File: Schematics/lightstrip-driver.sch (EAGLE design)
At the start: 11 parts, among them IC1 MCP2300X/P, Q1 FQP30N06L, Q2 FQP30N06L, Q3 FQP30N06L

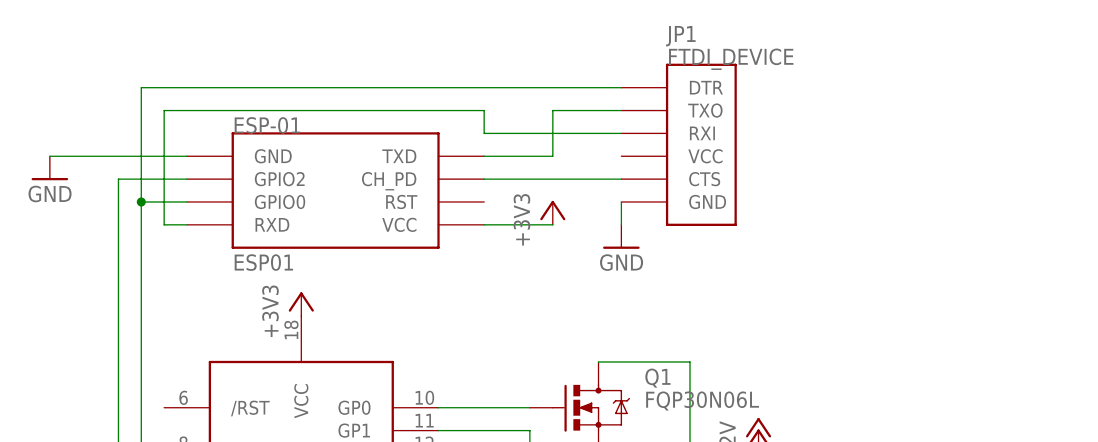
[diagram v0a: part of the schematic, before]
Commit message: Update board with correct ESP8266 autoreset connections
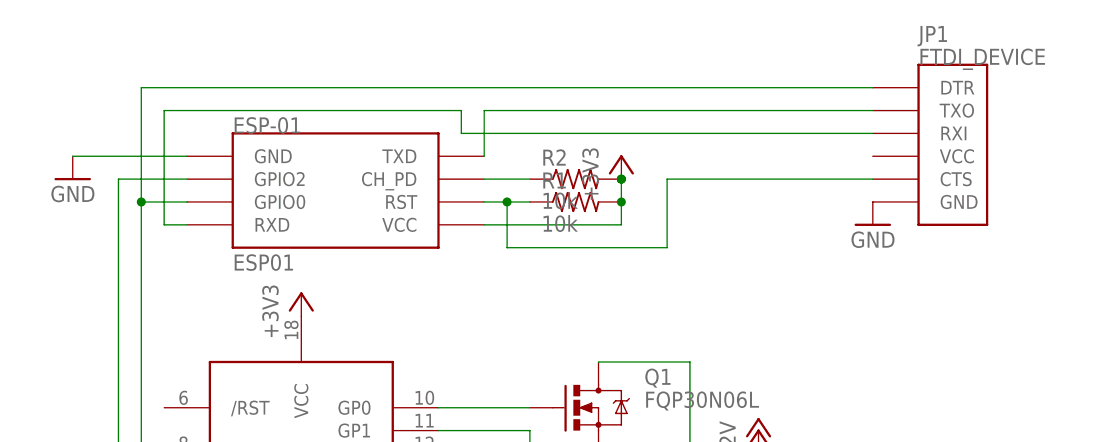
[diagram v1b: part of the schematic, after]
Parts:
- added R1, R2: 10k, resistor:R-US_0207/7
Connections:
- removed net N$10: ESP-01.CH_PD, JP1.CTS
- new net N$15: ESP-01.RST, JP1.CTS, R1.1
- new net N$3: ESP-01.CH_PD, R2.1
- net +3V3: now also R1.2, R2.2
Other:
- moved on the sheet: JP1
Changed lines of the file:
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@@
 <part name="GND9" library="supply1" deviceset="GND" device=""/>
 <part name="DC-IN" library="SparkFun-Connectors" deviceset="POWER_JACK" device="PTH"/>
+<part name="R1" library="resistor" deviceset="R-US_" device="0207/7" value="10k"/>
+<part name="R2" library="resistor" deviceset="R-US_" device="0207/7" value="10k"/>
 </parts>
 <sheets>
@@
 <instance part="+3V1" gate="G$1" x="-15.24" y="30.48"/>
 <instance part="GND2" gate="1" x="-25.4" y="15.24"/>
-<instance part="+3V2" gate="G$1" x="-55.88" y="104.14"/>
-<instance part="JP1" gate="G$1" x="-43.18" y="111.76"/>
-<instance part="GND3" gate="1" x="-48.26" y="99.06" rot="MR0"/>
+<instance part="+3V2" gate="G$1" x="-48.26" y="109.22"/>
+<instance part="JP1" gate="G$1" x="-15.24" y="111.76"/>
+<instance part="GND3" gate="1" x="-20.32" y="101.6" rot="MR0"/>
 <instance part="RGB" gate="G$1" x="-27.94" y="71.12" rot="R180"/>
 <instance part="P+2" gate="1" x="-33.02" y="78.74"/>
@@
 <instance part="P+4" gate="1" x="-76.2" y="22.86"/>
 <instance part="GND8" gate="1" x="-76.2" y="12.7"/>
-<instance part="GND9" gate="1" x="-111.76" y="106.68" rot="MR0"/>
+<instance part="GND9" gate="1" x="-109.22" y="106.68" rot="MR0"/>
 <instance part="DC-IN" gate="G$1" x="-45.72" y="15.24"/>
+<instance part="R1" gate="G$1" x="-53.34" y="104.14"/>
+<instance part="R2" gate="G$1" x="-53.34" y="106.68"/>
 </instances>
 <busses>
@@
 <pinref part="JP1" gate="G$1" pin="GND"/>
 <pinref part="GND3" gate="1" pin="GND"/>
-<wire x1="-48.26" y1="104.14" x2="-48.26" y2="101.6" width="0.1524" layer="91"/>
 </segment>
 <segment>
@@
 <pinref part="GND9" gate="1" pin="GND"/>
 <pinref part="ESP-01" gate="G$1" pin="GND"/>
-<wire x1="-111.76" y1="109.22" x2="-96.52" y2="109.22" width="0.1524" layer="91"/>
+<wire x1="-109.22" y1="109.22" x2="-96.52" y2="109.22" width="0.1524" layer="91"/>
 </segment>
 </net>
@@
 </segment>
 <segment>
-<pinref part="ESP-01" gate="G$1" pin="VCC"/>
-<pinref part="+3V2" gate="G$1" pin="+3V3"/>
-<wire x1="-63.5" y1="101.6" x2="-55.88" y2="101.6" width="0.1524" layer="91"/>
-</segment>
-<segment>
 <pinref part="IC1" gate="G$1" pin="VCC"/>
 <pinref part="+3V3" gate="G$1" pin="+3V3"/>
+</segment>
+<segment>
+<pinref part="+3V2" gate="G$1" pin="+3V3"/>
+<junction x="-48.26" y="106.68"/>
+<pinref part="R2" gate="G$1" pin="2"/>
+<wire x1="-48.26" y1="106.68" x2="-48.26" y2="104.14" width="0.1524" layer="91"/>
+<junction x="-48.26" y="106.68"/>
+<pinref part="R1" gate="G$1" pin="2"/>
+<pinref part="ESP-01" gate="G$1" pin="VCC"/>
+<wire x1="-63.5" y1="101.6" x2="-48.26" y2="101.6" width="0.1524" layer="91"/>
+<wire x1="-48.26" y1="101.6" x2="-48.26" y2="104.14" width="0.1524" layer="91"/>
+<junction x="-48.26" y="104.14"/>
 </segment>
 </net>
@@
 <wire x1="-96.52" y1="101.6" x2="-99.06" y2="101.6" width="0.1524" layer="91"/>
 <wire x1="-99.06" y1="101.6" x2="-99.06" y2="114.3" width="0.1524" layer="91"/>
-<wire x1="-99.06" y1="114.3" x2="-63.5" y2="114.3" width="0.1524" layer="91"/>
-<wire x1="-63.5" y1="114.3" x2="-63.5" y2="111.76" width="0.1524" layer="91"/>
-<wire x1="-63.5" y1="111.76" x2="-48.26" y2="111.76" width="0.1524" layer="91"/>
+<wire x1="-99.06" y1="114.3" x2="-66.04" y2="114.3" width="0.1524" layer="91"/>
+<wire x1="-66.04" y1="114.3" x2="-66.04" y2="111.76" width="0.1524" layer="91"/>
+<wire x1="-66.04" y1="111.76" x2="-20.32" y2="111.76" width="0.1524" layer="91"/>
 </segment>
 </net>
@@
 <segment>
 <pinref part="ESP-01" gate="G$1" pin="TXD"/>
-<wire x1="-63.5" y1="109.22" x2="-55.88" y2="109.22" width="0.1524" layer="91"/>
-<wire x1="-55.88" y1="109.22" x2="-55.88" y2="114.3" width="0.1524" layer="91"/>
-<wire x1="-55.88" y1="114.3" x2="-48.26" y2="114.3" width="0.1524" layer="91"/>
+<wire x1="-63.5" y1="109.22" x2="-63.5" y2="114.3" width="0.1524" layer="91"/>
+<wire x1="-63.5" y1="114.3" x2="-20.32" y2="114.3" width="0.1524" layer="91"/>
 <pinref part="JP1" gate="G$1" pin="TXO"/>
-</segment>
-</net>
-<net name="N$10" class="0">
-<segment>
-<pinref part="JP1" gate="G$1" pin="CTS"/>
-<pinref part="ESP-01" gate="G$1" pin="CH_PD"/>
-<wire x1="-48.26" y1="106.68" x2="-63.5" y2="106.68" width="0.1524" layer="91"/>
 </segment>
 </net>
@@
 <wire x1="-101.6" y1="116.84" x2="-101.6" y2="104.14" width="0.1524" layer="91"/>
 <junction x="-101.6" y="104.14"/>
-<wire x1="-101.6" y1="116.84" x2="-48.26" y2="116.84" width="0.1524" layer="91"/>
+<wire x1="-101.6" y1="116.84" x2="-20.32" y2="116.84" width="0.1524" layer="91"/>
 <pinref part="JP1" gate="G$1" pin="DTR"/>
 </segment>
@@
 </segment>
 </net>
+<net name="N$3" class="0">
+<segment>
+<pinref part="ESP-01" gate="G$1" pin="CH_PD"/>
+<pinref part="R2" gate="G$1" pin="1"/>
+<wire x1="-58.42" y1="106.68" x2="-63.5" y2="106.68" width="0.1524" layer="91"/>
+</segment>
+</net>
+<net name="N$15" class="0">
+<segment>
+<pinref part="ESP-01" gate="G$1" pin="RST"/>
+<pinref part="R1" gate="G$1" pin="1"/>
+<wire x1="-63.5" y1="104.14" x2="-60.96" y2="104.14" width="0.1524" layer="91"/>
+<wire x1="-60.96" y1="104.14" x2="-58.42" y2="104.14" width="0.1524" layer="91"/>
+<wire x1="-60.96" y1="104.14" x2="-60.96" y2="99.06" width="0.1524" layer="91"/>
+<junction x="-60.96" y="104.14"/>
+<pinref part="JP1" gate="G$1" pin="CTS"/>
+<wire x1="-43.18" y1="106.68" x2="-20.32" y2="106.68" width="0.1524" layer="91"/>
+<wire x1="-60.96" y1="99.06" x2="-43.18" y2="99.06" width="0.1524" layer="91"/>
+<wire x1="-43.18" y1="99.06" x2="-43.18" y2="106.68" width="0.1524" layer="91"/>
+</segment>
+</net>

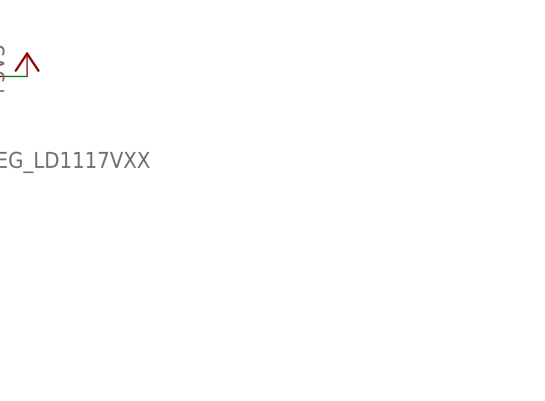
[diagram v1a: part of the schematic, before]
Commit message: Add mounting holes
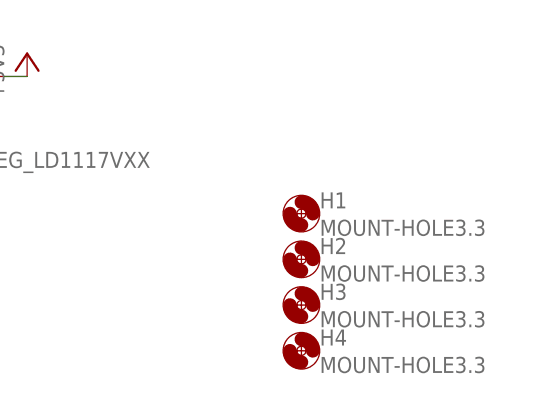
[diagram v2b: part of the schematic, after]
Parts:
- added H1, H2, H3, H4: MOUNT-HOLE3.3, holes:MOUNT-HOLE3.3
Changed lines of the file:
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@@
 <part name="R1" library="resistor" deviceset="R-US_" device="0207/7" value="10k"/>
 <part name="R2" library="resistor" deviceset="R-US_" device="0207/7" value="10k"/>
+<part name="H1" library="holes" deviceset="MOUNT-HOLE" device="3.3"/>
+<part name="H2" library="holes" deviceset="MOUNT-HOLE" device="3.3"/>
+<part name="H3" library="holes" deviceset="MOUNT-HOLE" device="3.3"/>
+<part name="H4" library="holes" deviceset="MOUNT-HOLE" device="3.3"/>
 </parts>
 <sheets>
@@
 <instance part="R1" gate="G$1" x="-53.34" y="104.14"/>
 <instance part="R2" gate="G$1" x="-53.34" y="106.68"/>
+<instance part="H1" gate="G$1" x="15.24" y="12.7"/>
+<instance part="H2" gate="G$1" x="15.24" y="7.62"/>
+<instance part="H3" gate="G$1" x="15.24" y="2.54"/>
+<instance part="H4" gate="G$1" x="15.24" y="-2.54"/>
 </instances>
 <busses>
